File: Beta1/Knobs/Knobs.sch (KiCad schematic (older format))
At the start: 44 parts, among them U1000 MCP3008T-I/SL, U2 MCP3008T-I/SL

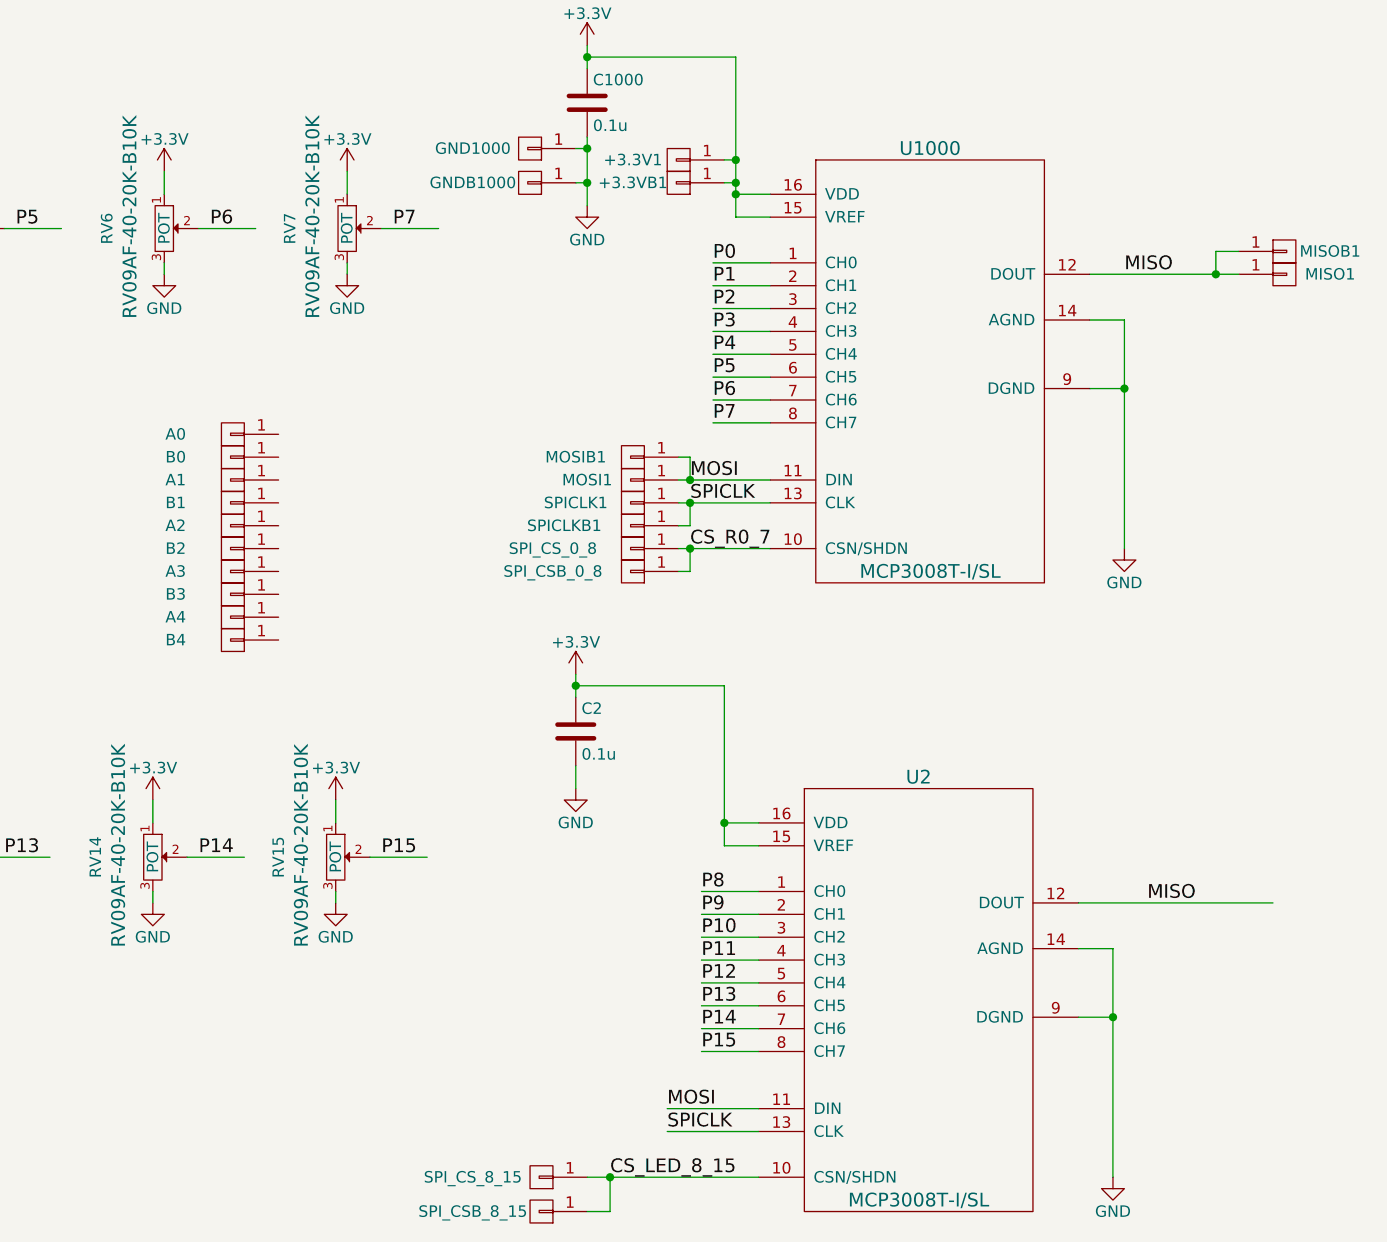
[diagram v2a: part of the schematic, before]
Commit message: Reduced Height, Moved TH, Holes, SMT Chips, Rerouted.
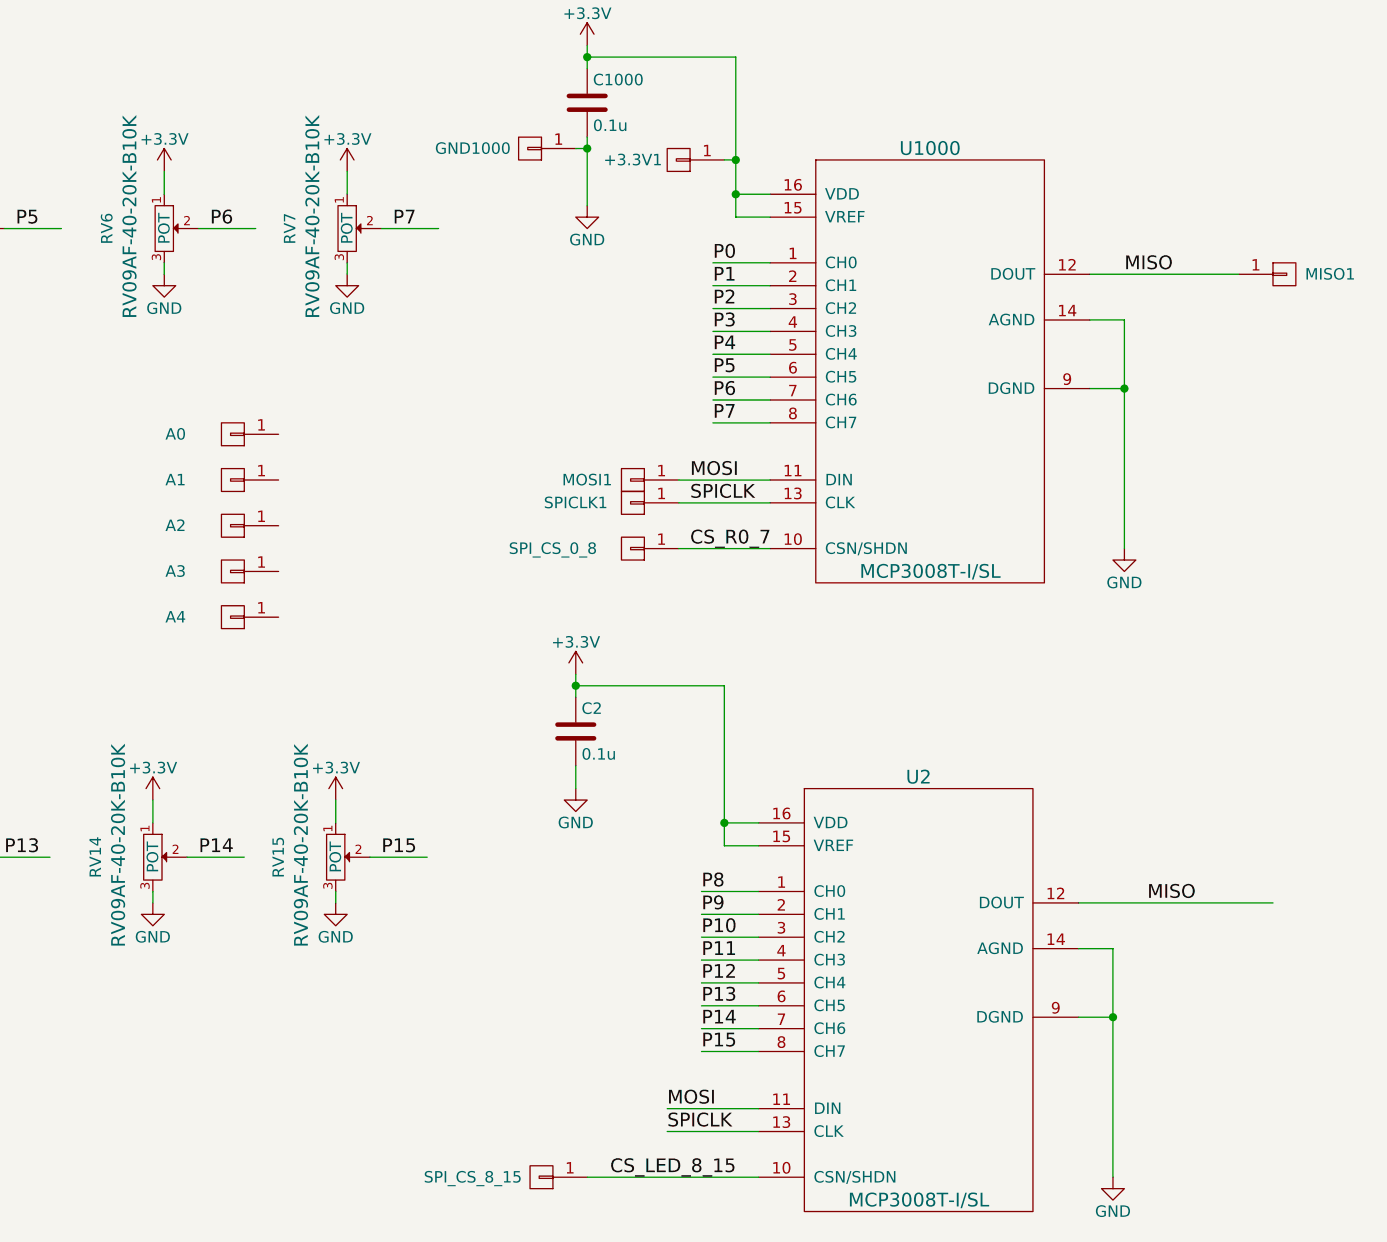
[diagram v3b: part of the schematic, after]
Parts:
- removed +3.3VB1, B0, B1, B2, B3, B4, GNDB1000, MISOB1, MOSIB1, SPICLKB1, SPI_CSB_0_8, SPI_CSB_8_15: CONN_01X01, Liberry:single_0.1, symbol CONN_01X01
- +3.3V1, A0, A1, A2, A3, A4, GND1000, MISO1, MOSI1, SPICLK1, SPI_CS_0_8, SPI_CS_8_15: footprint Liberry:single_0.1 -> Liberry:TH_0.1_1x2_Jumper
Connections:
- wire segments 104 -> 92
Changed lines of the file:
@@
 F 0 "MOSI1" H 9400 2650 50  0000 C CNN
 F 1 "CONN_01X01" V 9300 2650 50  0001 C CNN
-F 2 "Liberry:single_0.1" H 9200 2650 50  0001 C CNN
+F 2 "Liberry:TH_0.1_1x2_Jumper" H 9200 2650 50  0001 C CNN
 F 3 "" H 9200 2650 50  0000 C CNN
 F 4 "PCB" H 9200 2650 60  0001 C CNN "MFG"
@@
 F 0 "SPICLK1" H 9450 2750 50  0000 C CNN
 F 1 "CONN_01X01" V 9300 2750 50  0001 C CNN
-F 2 "Liberry:single_0.1" H 9200 2750 50  0001 C CNN
+F 2 "Liberry:TH_0.1_1x2_Jumper" H 9200 2750 50  0001 C CNN
 F 3 "" H 9200 2750 50  0000 C CNN
 F 4 "PCB" H 9200 2750 60  0001 C CNN "MFG"
@@
 F 0 "SPI_CS_0_8" H 9550 2950 50  0000 C CNN
 F 1 "CONN_01X01" V 9300 2950 50  0001 C CNN
-F 2 "Liberry:single_0.1" H 9200 2950 50  0001 C CNN
+F 2 "Liberry:TH_0.1_1x2_Jumper" H 9200 2950 50  0001 C CNN
 F 3 "" H 9200 2950 50  0000 C CNN
 F 4 "PCB" H 9200 2950 60  0001 C CNN "MFG"
@@
 F 0 "MISO1" H 12250 1750 50  0000 C CNN
 F 1 "CONN_01X01" V 12150 1750 50  0001 C CNN
-F 2 "Liberry:single_0.1" H 12050 1750 50  0001 C CNN
+F 2 "Liberry:TH_0.1_1x2_Jumper" H 12050 1750 50  0001 C CNN
 F 3 "" H 12050 1750 50  0000 C CNN
 F 4 "PCB" H 12050 1750 60  0001 C CNN "MFG"
@@
 F 0 "+3.3V1" H 9600 1250 50  0000 C CNN
 F 1 "CONN_01X01" V 9500 1250 50  0001 C CNN
-F 2 "Liberry:single_0.1" H 9400 1250 50  0001 C CNN
+F 2 "Liberry:TH_0.1_1x2_Jumper" H 9400 1250 50  0001 C CNN
 F 3 "" H 9400 1250 50  0000 C CNN
 F 4 "PCB" H 9400 1250 60  0001 C CNN "MFG"
@@
 F 0 "GND1000" H 9000 1200 50  0000 C CNN
 F 1 "CONN_01X01" V 8850 1200 50  0001 C CNN
-F 2 "Liberry:single_0.1" H 8750 1200 50  0001 C CNN
+F 2 "Liberry:TH_0.1_1x2_Jumper" H 8750 1200 50  0001 C CNN
 F 3 "" H 8750 1200 50  0000 C CNN
 F 4 "PCB" H 8750 1200 60  0001 C CNN "MFG"
@@
 F 0 "SPI_CS_8_15" H 9100 5700 50  0000 C CNN
 F 1 "CONN_01X01" V 8900 5700 50  0001 C CNN
-F 2 "Liberry:single_0.1" H 8800 5700 50  0001 C CNN
+F 2 "Liberry:TH_0.1_1x2_Jumper" H 8800 5700 50  0001 C CNN
 F 3 "" H 8800 5700 50  0000 C CNN
 F 4 "PCB" H 8800 5700 60  0001 C CNN "MFG"
@@
 MISO
 $Comp
-L CONN_01X01 GNDB1000
-U 1 1 5832E879
-P 8750 1350
-F 0 "GNDB1000" H 9000 1350 50  0000 C CNN
-F 1 "CONN_01X01" V 8850 1350 50  0001 C CNN
-F 2 "Liberry:single_0.1" H 8750 1350 50  0001 C CNN
-F 3 "" H 8750 1350 50  0000 C CNN
-F 4 "PCB" H 8750 1350 60  0001 C CNN "MFG"
-F 5 "ON_PCB" H 8750 1350 60  0001 C CNN "MPN"
-	1    8750 1350
-	-1   0    0    1
-$EndComp
-$Comp
-L CONN_01X01 +3.3VB1
-U 1 1 5832E8E1
-P 9400 1350
-F 0 "+3.3VB1" H 9600 1350 50  0000 C CNN
-F 1 "CONN_01X01" V 9500 1350 50  0001 C CNN
-F 2 "Liberry:single_0.1" H 9400 1350 50  0001 C CNN
-F 3 "" H 9400 1350 50  0000 C CNN
-F 4 "PCB" H 9400 1350 60  0001 C CNN "MFG"
-F 5 "ON_PCB" H 9400 1350 60  0001 C CNN "MPN"
-	1    9400 1350
-	-1   0    0    1
-$EndComp
-$Comp
-L CONN_01X01 MOSIB1
-U 1 1 5832EC50
-P 9200 2550
-F 0 "MOSIB1" H 9450 2550 50  0000 C CNN
-F 1 "CONN_01X01" V 9300 2550 50  0001 C CNN
-F 2 "Liberry:single_0.1" H 9200 2550 50  0001 C CNN
-F 3 "" H 9200 2550 50  0000 C CNN
-F 4 "PCB" H 9200 2550 60  0001 C CNN "MFG"
-F 5 "ON_PCB" H 9200 2550 60  0001 C CNN "MPN"
-	1    9200 2550
-	-1   0    0    1
-$EndComp
-$Comp
-L CONN_01X01 SPICLKB1
-U 1 1 5832ECC2
-P 9200 2850
-F 0 "SPICLKB1" H 9500 2850 50  0000 C CNN
-F 1 "CONN_01X01" V 9300 2850 50  0001 C CNN
-F 2 "Liberry:single_0.1" H 9200 2850 50  0001 C CNN
-F 3 "" H 9200 2850 50  0000 C CNN
-F 4 "PCB" H 9200 2850 60  0001 C CNN "MFG"
-F 5 "ON_PCB" H 9200 2850 60  0001 C CNN "MPN"
-	1    9200 2850
-	-1   0    0    1
-$EndComp
-$Comp
-L CONN_01X01 SPI_CSB_0_8
-U 1 1 5832ED37
-P 9200 3050
-F 0 "SPI_CSB_0_8" H 9550 3050 50  0000 C CNN
-F 1 "CONN_01X01" V 9300 3050 50  0001 C CNN
-F 2 "Liberry:single_0.1" H 9200 3050 50  0001 C CNN
-F 3 "" H 9200 3050 50  0000 C CNN
-F 4 "PCB" H 9200 3050 60  0001 C CNN "MFG"
-F 5 "ON_PCB" H 9200 3050 60  0001 C CNN "MPN"
-	1    9200 3050
-	-1   0    0    1
-$EndComp
-$Comp
-L CONN_01X01 MISOB1
-U 1 1 5832F20B
-P 12050 1650
-F 0 "MISOB1" H 12250 1650 50  0000 C CNN
-F 1 "CONN_01X01" V 12150 1650 50  0001 C CNN
-F 2 "Liberry:single_0.1" H 12050 1650 50  0001 C CNN
-F 3 "" H 12050 1650 50  0000 C CNN
-F 4 "PCB" H 12050 1650 60  0001 C CNN "MFG"
-F 5 "ON_PCB" H 12050 1650 60  0001 C CNN "MPN"
-	1    12050 1650
-	1    0    0    -1
-$EndComp
-Wire Wire Line
-	11850 1650 11750 1650
-Wire Wire Line
-	11750 1650 11750 1750
-Connection ~ 11750 1750
-Wire Wire Line
-	9400 2550 9450 2550
-Wire Wire Line
-	9450 2550 9450 2650
-Connection ~ 9450 2650
-Wire Wire Line
-	9400 2850 9450 2850
-Wire Wire Line
-	9450 2850 9450 2750
-Connection ~ 9450 2750
-Wire Wire Line
-	9400 3050 9450 3050
-Wire Wire Line
-	9450 3050 9450 2950
-Connection ~ 9450 2950
-Wire Wire Line
-	9600 1350 9650 1350
-Connection ~ 9650 1350
-Wire Wire Line
-	8950 1350 9000 1350
-Connection ~ 9000 1350
-$Comp
-L CONN_01X01 SPI_CSB_8_15
-U 1 1 583313D9
-P 8800 5850
-F 0 "SPI_CSB_8_15" H 9100 5850 50  0000 C CNN
-F 1 "CONN_01X01" V 8900 5850 50  0001 C CNN
-F 2 "Liberry:single_0.1" H 8800 5850 50  0001 C CNN
-F 3 "" H 8800 5850 50  0000 C CNN
-F 4 "PCB" H 8800 5850 60  0001 C CNN "MFG"
-F 5 "ON_PCB" H 8800 5850 60  0001 C CNN "MPN"
-	1    8800 5850
-	-1   0    0    1
-$EndComp
-Wire Wire Line
-	9000 5850 9100 5850
-Wire Wire Line
-	9100 5850 9100 5700
-Connection ~ 9100 5700
-$Comp
 L CONN_01X01 A0
 U 1 1 58336F43
@@
 F 0 "A0" H 7700 2450 50  0000 C CNN
 F 1 "CONN_01X01" V 7550 2450 50  0001 C CNN
-F 2 "Liberry:single_0.1" H 7450 2450 50  0001 C CNN
+F 2 "Liberry:TH_0.1_1x2_Jumper" H 7450 2450 50  0001 C CNN
 F 3 "" H 7450 2450 50  0000 C CNN
 F 4 "PCB" H 7450 2450 60  0001 C CNN "MFG"
 F 5 "ON_PCB" H 7450 2450 60  0001 C CNN "MPN"
 	1    7450 2450
-	-1   0    0    1
-$EndComp
-$Comp
-L CONN_01X01 B0
-U 1 1 583370FC
-P 7450 2550
-F 0 "B0" H 7700 2550 50  0000 C CNN
-F 1 "CONN_01X01" V 7550 2550 50  0001 C CNN
-F 2 "Liberry:single_0.1" H 7450 2550 50  0001 C CNN
-F 3 "" H 7450 2550 50  0000 C CNN
-F 4 "PCB" H 7450 2550 60  0001 C CNN "MFG"
-F 5 "ON_PCB" H 7450 2550 60  0001 C CNN "MPN"
-	1    7450 2550
 	-1   0    0    1
 $EndComp
@@
 F 0 "A1" H 7700 2650 50  0000 C CNN
 F 1 "CONN_01X01" V 7550 2650 50  0001 C CNN
-F 2 "Liberry:single_0.1" H 7450 2650 50  0001 C CNN
+F 2 "Liberry:TH_0.1_1x2_Jumper" H 7450 2650 50  0001 C CNN
 F 3 "" H 7450 2650 50  0000 C CNN
 F 4 "PCB" H 7450 2650 60  0001 C CNN "MFG"
 F 5 "ON_PCB" H 7450 2650 60  0001 C CNN "MPN"
 	1    7450 2650
-	-1   0    0    1
-$EndComp
-$Comp
-L CONN_01X01 B1
-U 1 1 58337207
-P 7450 2750
-F 0 "B1" H 7700 2750 50  0000 C CNN
-F 1 "CONN_01X01" V 7550 2750 50  0001 C CNN
-F 2 "Liberry:single_0.1" H 7450 2750 50  0001 C CNN
-F 3 "" H 7450 2750 50  0000 C CNN
-F 4 "PCB" H 7450 2750 60  0001 C CNN "MFG"
-F 5 "ON_PCB" H 7450 2750 60  0001 C CNN "MPN"
-	1    7450 2750
 	-1   0    0    1
 $EndComp
@@
 F 0 "A2" H 7700 2850 50  0000 C CNN
 F 1 "CONN_01X01" V 7550 2850 50  0001 C CNN
-F 2 "Liberry:single_0.1" H 7450 2850 50  0001 C CNN
+F 2 "Liberry:TH_0.1_1x2_Jumper" H 7450 2850 50  0001 C CNN
 F 3 "" H 7450 2850 50  0000 C CNN
 F 4 "PCB" H 7450 2850 60  0001 C CNN "MFG"
 F 5 "ON_PCB" H 7450 2850 60  0001 C CNN "MPN"
 	1    7450 2850
-	-1   0    0    1
-$EndComp
-$Comp
-L CONN_01X01 B2
-U 1 1 58337611
-P 7450 2950
-F 0 "B2" H 7700 2950 50  0000 C CNN
-F 1 "CONN_01X01" V 7550 2950 50  0001 C CNN
-F 2 "Liberry:single_0.1" H 7450 2950 50  0001 C CNN
-F 3 "" H 7450 2950 50  0000 C CNN
-F 4 "PCB" H 7450 2950 60  0001 C CNN "MFG"
-F 5 "ON_PCB" H 7450 2950 60  0001 C CNN "MPN"
-	1    7450 2950
 	-1   0    0    1
 $EndComp
@@
 F 0 "A3" H 7700 3050 50  0000 C CNN
 F 1 "CONN_01X01" V 7550 3050 50  0001 C CNN
-F 2 "Liberry:single_0.1" H 7450 3050 50  0001 C CNN
+F 2 "Liberry:TH_0.1_1x2_Jumper" H 7450 3050 50  0001 C CNN
 F 3 "" H 7450 3050 50  0000 C CNN
 F 4 "PCB" H 7450 3050 60  0001 C CNN "MFG"
 F 5 "ON_PCB" H 7450 3050 60  0001 C CNN "MPN"
 	1    7450 3050
-	-1   0    0    1
-$EndComp
-$Comp
-L CONN_01X01 B3
-U 1 1 58337621
-P 7450 3150
-F 0 "B3" H 7700 3150 50  0000 C CNN
-F 1 "CONN_01X01" V 7550 3150 50  0001 C CNN
-F 2 "Liberry:single_0.1" H 7450 3150 50  0001 C CNN
-F 3 "" H 7450 3150 50  0000 C CNN
-F 4 "PCB" H 7450 3150 60  0001 C CNN "MFG"
-F 5 "ON_PCB" H 7450 3150 60  0001 C CNN "MPN"
-	1    7450 3150
 	-1   0    0    1
 $EndComp
@@
 F 0 "A4" H 7700 3250 50  0000 C CNN
 F 1 "CONN_01X01" V 7550 3250 50  0001 C CNN
-F 2 "Liberry:single_0.1" H 7450 3250 50  0001 C CNN
+F 2 "Liberry:TH_0.1_1x2_Jumper" H 7450 3250 50  0001 C CNN
 F 3 "" H 7450 3250 50  0000 C CNN
 F 4 "PCB" H 7450 3250 60  0001 C CNN "MFG"
@@
 	-1   0    0    1
 $EndComp
-$Comp
-L CONN_01X01 B4
-U 1 1 58337C29
-P 7450 3350
-F 0 "B4" H 7700 3350 50  0000 C CNN
-F 1 "CONN_01X01" V 7550 3350 50  0001 C CNN
-F 2 "Liberry:single_0.1" H 7450 3350 50  0001 C CNN
-F 3 "" H 7450 3350 50  0000 C CNN
-F 4 "PCB" H 7450 3350 60  0001 C CNN "MFG"
-F 5 "ON_PCB" H 7450 3350 60  0001 C CNN "MPN"
-	1    7450 3350
-	-1   0    0    1
-$EndComp
